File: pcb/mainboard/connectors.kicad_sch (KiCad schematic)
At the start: 20 parts, among them J28 SMPM, J29 SMPM, J30 SMPM, J31 SMPM, J32 SMPM, J33 SMPM, J34 SMPM, J35 SMPM, J36 SMPM, J37 SMPM, J38 SMPM, J39 SMPM, J40 SMPM, J41 SMPM, J42 SMPM, J43 SMPM, J44 SMPM, J45 SMPM, J46 SMPM, J47 SMPM

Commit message: Finished initial iteration of schematic, needs a verification pass to check for missing features then schematic review
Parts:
- added C209, C210, C215, C216: 0.47 uF, symbol device:C
- added C211, C212, C217, C218: 4.7 uF, symbol device:C
- added C213, C214, C219, C220: 10 uF, symbol device:C
- added K1, K2, K3, K4: RELAY_TE_HF3_96, symbol special-azonenberg:RELAY_TE_HF3_96
- added U55, U56, U57, U58: BD63573NUV, symbol special-azonenberg:BD63573NUV
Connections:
- net GND: now also C209.2, C210.2, C211.2, C212.2, C213.2, C214.2, C215.2, C216.2, C217.2, C218.2, C219.2, C220.2, K1.10 (GND), K1.13 (GND), K1.2 (GND), K1.5 (GND), K1.7 (GND), K2.10 (GND), K2.13 (GND), K2.2 (GND), K2.5 (GND), K2.7 (GND), K3.10 (GND), K3.13 (GND), K3.2 (GND), K3.5 (GND), K3.7 (GND), K4.10 (GND), K4.13 (GND), K4.2 (GND), K4.5 (GND), K4.7 (GND), U55.10 (GND), U55.5 (PGND), U55.9 (PWM), U56.10 (GND), U56.5 (PGND), U56.9 (PWM), U57.10 (GND), U57.5 (PGND), U57.9 (PWM), U58.10 (GND), U58.5 (PGND), U58.9 (PWM)
- net IN10: now also K3.14 (A)
- net IN11: now also K4.14 (A)
- net IN8: now also K1.14 (A)
- net IN9: now also K2.14 (A)
- net IO10: now also K3.6 (COM)
- net IO11: now also K4.6 (COM)
- net IO8: now also K1.6 (COM)
- net IO9: now also K2.6 (COM)
- net OUT10: now also K3.20 (B)
- net OUT11: now also K4.20 (B)
- net OUT8: now also K1.20 (B)
- net OUT9: now also K2.20 (B)
- new net: K3.15 (GND), K3.17 (GND), K3.19 (GND), K3.21 (GND)
- new net: K2.15 (GND), K2.17 (GND), K2.19 (GND), K2.21 (GND)
- new net: K4.15 (GND), K4.17 (GND), K4.19 (GND), K4.21 (GND)
- new net: K1.15 (GND), K1.17 (GND), K1.19 (GND), K1.21 (GND)
- new net 12V0: C213.1, C214.1, C219.1, C220.1, U55.7 (VM), U56.7 (VM), U57.7 (VM), U58.7 (VM)
- new net 3V3: C209.1, C210.1, C211.1, C212.1, C215.1, C216.1, C217.1, C218.1, U55.1 (PS), U55.8 (VCC), U56.1 (PS), U56.8 (VCC), U57.1 (PS), U57.8 (VCC), U58.1 (PS), U58.8 (VCC)
- new net CH10_COIL_N: K3.1 (SET1_N), K3.12 (SET2_N), U55.4 (OUTB)
- new net CH10_COIL_P: K3.11 (SET1_P), K3.22 (SET2_P), U55.6 (OUTA)
- new net CH11_COIL_N: K4.1 (SET1_N), K4.12 (SET2_N), U57.4 (OUTB)
- new net CH11_COIL_P: K4.11 (SET1_P), K4.22 (SET2_P), U57.6 (OUTA)
- new net CH8_COIL_N: K1.1 (SET1_N), K1.12 (SET2_N), U56.4 (OUTB)
- new net CH8_COIL_P: K1.11 (SET1_P), K1.22 (SET2_P), U56.6 (OUTA)
- new net CH9_COIL_N: K2.1 (SET1_N), K2.12 (SET2_N), U58.4 (OUTB)
- new net CH9_COIL_P: K2.11 (SET1_P), K2.22 (SET2_P), U58.6 (OUTA)
- new net OE10A: U55.3 (INA)
- new net OE10B: U55.2 (INB)
- new net OE11A: U57.3 (INA)
- new net OE11B: U57.2 (INB)
- new net OE8A: U56.3 (INA)
- new net OE8B: U56.2 (INB)
- new net OE9A: U58.3 (INA)
- new net OE9B: U58.2 (INB)
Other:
- note removed: "TODO: Relays or something to mux bidir ports"
- moved on the sheet: J28, J29, J30, J31, J32, J33, J34, J35, J36, J37, J38, J39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

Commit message: Calculated power monitor voltage divider
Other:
- company: (none) -> Antikernel Labs
- title: (none) -> Trigger Crossbar
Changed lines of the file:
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@@
 (kicad_sch (version 20211123) (generator eeschema)
   (paper "A4")
+  (title_block
+    (title "Trigger Crossbar")
+    (date "2023-12-17")
+    (rev "0.1")
+    (company "Antikernel Labs")
+    (comment 1 "Andrew D. Zonenberg")
+  )
   (junction (at 133.35 124.46) (diameter 0) (color 0 0 0 0)
   )

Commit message: Began assigning footprints
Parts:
- C209, C210, C215, C216: footprint (none) -> azonenberg_pcb:EIA_0402_CAP_NOSILK
- C211, C212, C217, C218: footprint (none) -> azonenberg_pcb:EIA_0603_CAP_NOSILK
- C213, C214, C219, C220: value 10 uF -> 10 uF 25V; footprint (none) -> azonenberg_pcb:EIA_1210_CAP_NOSILK
- U55, U56, U57, U58: footprint (none) -> azonenberg_pcb:DFN_10_0.5MM_3x3MM
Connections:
- net GND: now also K1.15 (GND), K1.17 (GND), K1.19 (GND), K1.21 (GND), K2.15 (GND), K2.17 (GND), K2.19 (GND), K2.21 (GND), K3.15 (GND), K3.17 (GND), K3.19 (GND), K3.21 (GND), K4.15 (GND), K4.17 (GND), K4.19 (GND), K4.21 (GND)
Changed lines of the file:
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@@
+    (effects (font (size 1.27 1.27)) (justify left bottom))
+  )
+  (label "GND" (at 204.47 55.88 0)
     (effects (font (size 1.27 1.27)) (justify left bottom))
   )
@@
     (effects (font (size 1.27 1.27)) (justify right bottom))
   )
+  (label "GND" (at 204.47 22.86 0)
+    (effects (font (size 1.27 1.27)) (justify left bottom))
+  )
   (label "GND" (at 67.31 40.64 0)
     (effects (font (size 1.27 1.27)) (justify left bottom))
@@
     (effects (font (size 1.27 1.27)) (justify left bottom))
   )
+  (label "GND" (at 142.24 55.88 0)
+    (effects (font (size 1.27 1.27)) (justify left bottom))
+  )
   (label "3V3" (at 177.8 143.51 180)
     (effects (font (size 1.27 1.27)) (justify right bottom))
@@
   )
   (label "CH11_COIL_P" (at 200.66 146.05 0)
+    (effects (font (size 1.27 1.27)) (justify left bottom))
+  )
+  (label "GND" (at 142.24 22.86 0)
     (effects (font (size 1.27 1.27)) (justify left bottom))
   )
@@
       (effects (font (size 1.27 1.27)) (justify left))
     )
-    (property "Value" "10 uF" (id 1) (at 215.011 121.0822 0)
-      (effects (font (size 1.27 1.27)) (justify left))
-    )
-    (property "Footprint" "" (id 2) (at 213.0552 123.19 0)
+    (property "Value" "10 uF 25V" (id 1) (at 215.011 121.0822 0)
+      (effects (font (size 1.27 1.27)) (justify left))
+    )
+    (property "Footprint" "azonenberg_pcb:EIA_1210_CAP_NOSILK" (id 2) (at 213.0552 123.19 0)
       (effects (font (size 1.27 1.27)) hide)
     )
@@
       (effects (font (size 1.27 1.27)) (justify left))
     )
-    (property "Value" "10 uF" (id 1) (at 213.741 160.4522 0)
-      (effects (font (size 1.27 1.27)) (justify left))
-    )
-    (property "Footprint" "" (id 2) (at 211.7852 162.56 0)
+    (property "Value" "10 uF 25V" (id 1) (at 213.741 160.4522 0)
+      (effects (font (size 1.27 1.27)) (justify left))
+    )
+    (property "Footprint" "azonenberg_pcb:EIA_1210_CAP_NOSILK" (id 2) (at 211.7852 162.56 0)
       (effects (font (size 1.27 1.27)) hide)
     )
@@
     (property "Reference" "U58" (id 0) (at 190.5 86.521 0))
     (property "Value" "BD63573NUV" (id 1) (at 190.5 89.0579 0))
-    (property "Footprint" "" (id 2) (at 182.88 114.3 0)
+    (property "Footprint" "azonenberg_pcb:DFN_10_0.5MM_3x3MM" (id 2) (at 182.88 114.3 0)
       (effects (font (size 1.27 1.27)) hide)
     )
@@
       (effects (font (size 1.27 1.27)) (justify left))
     )
-    (property "Footprint" "" (id 2) (at 133.0452 163.83 0)
+    (property "Footprint" "azonenberg_pcb:EIA_0603_CAP_NOSILK" (id 2) (at 133.0452 163.83 0)
       (effects (font (size 1.27 1.27)) hide)
     )
@@
       (effects (font (size 1.27 1.27)) (justify left))
     )
-    (property "Value" "10 uF" (id 1) (at 152.781 122.3522 0)
-      (effects (font (size 1.27 1.27)) (justify left))
-    )
-    (property "Footprint" "" (id 2) (at 150.8252 124.46 0)
+    (property "Value" "10 uF 25V" (id 1) (at 152.781 122.3522 0)
+      (effects (font (size 1.27 1.27)) (justify left))
+    )
+    (property "Footprint" "azonenberg_pcb:EIA_1210_CAP_NOSILK" (id 2) (at 150.8252 124.46 0)
       (effects (font (size 1.27 1.27)) hide)
     )
@@
       (effects (font (size 1.27 1.27)) (justify left))
     )
-    (property "Footprint" "" (id 2) (at 120.3452 163.83 0)
+    (property "Footprint" "azonenberg_pcb:EIA_0402_CAP_NOSILK" (id 2) (at 120.3452 163.83 0)
       (effects (font (size 1.27 1.27)) hide)
     )
@@
     (property "Reference" "U55" (id 0) (at 127 127.161 0))
     (property "Value" "BD63573NUV" (id 1) (at 127 129.6979 0))
-    (property "Footprint" "" (id 2) (at 119.38 154.94 0)
+    (property "Footprint" "azonenberg_pcb:DFN_10_0.5MM_3x3MM" (id 2) (at 119.38 154.94 0)
       (effects (font (size 1.27 1.27)) hide)
     )
@@
       (effects (font (size 1.27 1.27)) (justify left))
     )
-    (property "Footprint" "" (id 2) (at 195.2752 162.56 0)
+    (property "Footprint" "azonenberg_pcb:EIA_0603_CAP_NOSILK" (id 2) (at 195.2752 162.56 0)
       (effects (font (size 1.27 1.27)) hide)
     )
@@
       (effects (font (size 1.27 1.27)) (justify left))
     )
-    (property "Footprint" "" (id 2) (at 134.3152 124.46 0)
+    (property "Footprint" "azonenberg_pcb:EIA_0603_CAP_NOSILK" (id 2) (at 134.3152 124.46 0)
       (effects (font (size 1.27 1.27)) hide)
     )
@@
       (effects (font (size 1.27 1.27)) (justify left))
     )
-    (property "Footprint" "" (id 2) (at 182.5752 162.56 0)
+    (property "Footprint" "azonenberg_pcb:EIA_0402_CAP_NOSILK" (id 2) (at 182.5752 162.56 0)
       (effects (font (size 1.27 1.27)) hide)
     )
@@
     (property "Reference" "U57" (id 0) (at 189.23 125.891 0))
     (property "Value" "BD63573NUV" (id 1) (at 189.23 128.4279 0))
-    (property "Footprint" "" (id 2) (at 181.61 153.67 0)
+    (property "Footprint" "azonenberg_pcb:DFN_10_0.5MM_3x3MM" (id 2) (at 181.61 153.67 0)
       (effects (font (size 1.27 1.27)) hide)
     )
@@
       (effects (font (size 1.27 1.27)) (justify left))
     )
-    (property "Footprint" "" (id 2) (at 196.5452 123.19 0)
+    (property "Footprint" "azonenberg_pcb:EIA_0603_CAP_NOSILK" (id 2) (at 196.5452 123.19 0)
       (effects (font (size 1.27 1.27)) hide)
     )
@@
       (effects (font (size 1.27 1.27)) (justify left))
     )
-    (property "Footprint" "" (id 2) (at 121.6152 124.46 0)
+    (property "Footprint" "azonenberg_pcb:EIA_0402_CAP_NOSILK" (id 2) (at 121.6152 124.46 0)
       (effects (font (size 1.27 1.27)) hide)
     )
@@
       (effects (font (size 1.27 1.27)) (justify left))
     )
-    (property "Footprint" "" (id 2) (at 183.8452 123.19 0)
+    (property "Footprint" "azonenberg_pcb:EIA_0402_CAP_NOSILK" (id 2) (at 183.8452 123.19 0)
       (effects (font (size 1.27 1.27)) hide)
     )
@@
       (effects (font (size 1.27 1.27)) (justify left))
     )
-    (property "Value" "10 uF" (id 1) (at 151.511 161.7222 0)
-      (effects (font (size 1.27 1.27)) (justify left))
-    )
-    (property "Footprint" "" (id 2) (at 149.5552 163.83 0)
+    (property "Value" "10 uF 25V" (id 1) (at 151.511 161.7222 0)
+      (effects (font (size 1.27 1.27)) (justify left))
+    )
+    (property "Footprint" "azonenberg_pcb:EIA_1210_CAP_NOSILK" (id 2) (at 149.5552 163.83 0)
       (effects (font (size 1.27 1.27)) hide)
     )
@@
     (property "Reference" "U56" (id 0) (at 128.27 87.791 0))
     (property "Value" "BD63573NUV" (id 1) (at 128.27 90.3279 0))
-    (property "Footprint" "" (id 2) (at 120.65 115.57 0)
-      (effects (font (size 1.27 1.27)) hide)
-    )
+    (property "Footprint" "azonenberg_pcb:DFN_10_0.5MM_3x3MM" (id 2) (at 120.65 115.57 0)
+      (effects (font (size 1.27 1.27)) hide)
+    )

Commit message: Finished component footprint assignment, started some EM simulations. Ready for schematic review.
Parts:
- J28, J29, J30, J31, J32, J33, J34, J35, J36, J37, J38, J39, J40, J41, J42, J43, J44, J45, J46, J47: footprint (none) -> azonenberg_pcb:CONN_SMPM_AMPHENOL_C925-197J-51PT
- K1, K2, K3, K4: footprint (none) -> azonenberg_pcb:RELAY_TE_HF3_2COIL_50OHM
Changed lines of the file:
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@@
   (title_block
     (title "Trigger Crossbar")
-    (date "2023-12-17")
+    (date "2023-12-18")
     (rev "0.1")
     (company "Antikernel Labs")
@@
     (property "Reference" "K3" (id 0) (at 191.77 17.941 0))
     (property "Value" "RELAY_TE_HF3_96" (id 1) (at 191.77 20.4779 0))
-    (property "Footprint" "" (id 2) (at 182.88 48.26 0)
+    (property "Footprint" "azonenberg_pcb:RELAY_TE_HF3_2COIL_50OHM" (id 2) (at 182.88 48.26 0)
       (effects (font (size 1.27 1.27)) hide)
     )
@@
     (property "Reference" "J34" (id 0) (at 35.5599 44.0036 0))
     (property "Value" "SMPM" (id 1) (at 35.5599 46.5405 0))
-    (property "Footprint" "" (id 2) (at 35.56 49.53 0)
+    (property "Footprint" "azonenberg_pcb:CONN_SMPM_AMPHENOL_C925-197J-51PT" (id 2) (at 35.56 49.53 0)
       (effects (font (size 1.27 1.27)) hide)
     )
@@
     (property "Reference" "J40" (id 0) (at 21.5899 74.4836 0))
     (property "Value" "SMPM" (id 1) (at 21.5899 77.0205 0))
-    (property "Footprint" "" (id 2) (at 21.59 80.01 0)
+    (property "Footprint" "azonenberg_pcb:CONN_SMPM_AMPHENOL_C925-197J-51PT" (id 2) (at 21.59 80.01 0)
       (effects (font (size 1.27 1.27)) hide)
     )
@@
     (property "Reference" "J28" (id 0) (at 21.5899 16.0636 0))
     (property "Value" "SMPM" (id 1) (at 21.5899 18.6005 0))
-    (property "Footprint" "" (id 2) (at 21.59 21.59 0)
+    (property "Footprint" "azonenberg_pcb:CONN_SMPM_AMPHENOL_C925-197J-51PT" (id 2) (at 21.59 21.59 0)
       (effects (font (size 1.27 1.27)) hide)
     )
@@
     (property "Reference" "J32" (id 0) (at 35.5599 16.0636 0))
     (property "Value" "SMPM" (id 1) (at 35.5599 18.6005 0))
-    (property "Footprint" "" (id 2) (at 35.56 21.59 0)
+    (property "Footprint" "azonenberg_pcb:CONN_SMPM_AMPHENOL_C925-197J-51PT" (id 2) (at 35.56 21.59 0)
       (effects (font (size 1.27 1.27)) hide)
     )
@@
     (property "Reference" "J45" (id 0) (at 50.7999 88.4536 0))
     (property "Value" "SMPM" (id 1) (at 50.7999 90.9905 0))
-    (property "Footprint" "" (id 2) (at 50.8 93.98 0)
+    (property "Footprint" "azonenberg_pcb:CONN_SMPM_AMPHENOL_C925-197J-51PT" (id 2) (at 50.8 93.98 0)
       (effects (font (size 1.27 1.27)) hide)
     )
@@
     (property "Reference" "J44" (id 0) (at 50.7999 74.4836 0))
     (property "Value" "SMPM" (id 1) (at 50.7999 77.0205 0))
-    (property "Footprint" "" (id 2) (at 50.8 80.01 0)
+    (property "Footprint" "azonenberg_pcb:CONN_SMPM_AMPHENOL_C925-197J-51PT" (id 2) (at 50.8 80.01 0)
       (effects (font (size 1.27 1.27)) hide)
     )
@@
     (property "Reference" "J31" (id 0) (at 21.5899 57.9736 0))
     (property "Value" "SMPM" (id 1) (at 21.5899 60.5105 0))
-    (property "Footprint" "" (id 2) (at 21.59 63.5 0)
+    (property "Footprint" "azonenberg_pcb:CONN_SMPM_AMPHENOL_C925-197J-51PT" (id 2) (at 21.59 63.5 0)
       (effects (font (size 1.27 1.27)) hide)
     )
@@
     (property "Reference" "J43" (id 0) (at 35.5599 88.4536 0))
     (property "Value" "SMPM" (id 1) (at 35.5599 90.9905 0))
-    (property "Footprint" "" (id 2) (at 35.56 93.98 0)
+    (property "Footprint" "azonenberg_pcb:CONN_SMPM_AMPHENOL_C925-197J-51PT" (id 2) (at 35.56 93.98 0)
       (effects (font (size 1.27 1.27)) hide)
     )
@@
     (property "Reference" "J41" (id 0) (at 21.5899 88.4536 0))
     (property "Value" "SMPM" (id 1) (at 21.5899 90.9905 0))
-    (property "Footprint" "" (id 2) (at 21.59 93.98 0)
+    (property "Footprint" "azonenberg_pcb:CONN_SMPM_AMPHENOL_C925-197J-51PT" (id 2) (at 21.59 93.98 0)
       (effects (font (size 1.27 1.27)) hide)
     )
@@
     (property "Reference" "J37" (id 0) (at 49.5299 30.0336 0))
     (property "Value" "SMPM" (id 1) (at 49.5299 32.5705 0))
-    (property "Footprint" "" (id 2) (at 49.53 35.56 0)
+    (property "Footprint" "azonenberg_pcb:CONN_SMPM_AMPHENOL_C925-197J-51PT" (id 2) (at 49.53 35.56 0)
       (effects (font (size 1.27 1.27)) hide)
     )
@@
     (property "Reference" "J35" (id 0) (at 35.5599 57.9736 0))
     (property "Value" "SMPM" (id 1) (at 35.5599 60.5105 0))
-    (property "Footprint" "" (id 2) (at 35.56 63.5 0)
+    (property "Footprint" "azonenberg_pcb:CONN_SMPM_AMPHENOL_C925-197J-51PT" (id 2) (at 35.56 63.5 0)
       (effects (font (size 1.27 1.27)) hide)
     )
@@
     (property "Reference" "J36" (id 0) (at 49.5299 16.0636 0))
     (property "Value" "SMPM" (id 1) (at 49.5299 18.6005 0))
-    (property "Footprint" "" (id 2) (at 49.53 21.59 0)
+    (property "Footprint" "azonenberg_pcb:CONN_SMPM_AMPHENOL_C925-197J-51PT" (id 2) (at 49.53 21.59 0)
       (effects (font (size 1.27 1.27)) hide)
     )
@@
     (property "Reference" "J46" (id 0) (at 63.4999 74.4836 0))
     (property "Value" "SMPM" (id 1) (at 63.4999 77.0205 0))
-    (property "Footprint" "" (id 2) (at 63.5 80.01 0)
+    (property "Footprint" "azonenberg_pcb:CONN_SMPM_AMPHENOL_C925-197J-51PT" (id 2) (at 63.5 80.01 0)
       (effects (font (size 1.27 1.27)) hide)
     )
@@
     (property "Reference" "J29" (id 0) (at 21.5899 30.0336 0))
     (property "Value" "SMPM" (id 1) (at 21.5899 32.5705 0))
-    (property "Footprint" "" (id 2) (at 21.59 35.56 0)
+    (property "Footprint" "azonenberg_pcb:CONN_SMPM_AMPHENOL_C925-197J-51PT" (id 2) (at 21.59 35.56 0)
       (effects (font (size 1.27 1.27)) hide)
     )
@@
     (property "Reference" "J42" (id 0) (at 35.5599 74.4836 0))
     (property "Value" "SMPM" (id 1) (at 35.5599 77.0205 0))
-    (property "Footprint" "" (id 2) (at 35.56 80.01 0)
+    (property "Footprint" "azonenberg_pcb:CONN_SMPM_AMPHENOL_C925-197J-51PT" (id 2) (at 35.56 80.01 0)
       (effects (font (size 1.27 1.27)) hide)
     )
@@
     (property "Reference" "J30" (id 0) (at 21.5899 44.0036 0))
     (property "Value" "SMPM" (id 1) (at 21.5899 46.5405 0))
-    (property "Footprint" "" (id 2) (at 21.59 49.53 0)
+    (property "Footprint" "azonenberg_pcb:CONN_SMPM_AMPHENOL_C925-197J-51PT" (id 2) (at 21.59 49.53 0)
       (effects (font (size 1.27 1.27)) hide)
     )
@@
     (property "Reference" "K2" (id 0) (at 129.54 50.961 0))
     (property "Value" "RELAY_TE_HF3_96" (id 1) (at 129.54 53.4979 0))
-    (property "Footprint" "" (id 2) (at 120.65 81.28 0)
+    (property "Footprint" "azonenberg_pcb:RELAY_TE_HF3_2COIL_50OHM" (id 2) (at 120.65 81.28 0)
       (effects (font (size 1.27 1.27)) hide)
     )
@@
     (property "Reference" "K4" (id 0) (at 191.77 50.961 0))
     (property "Value" "RELAY_TE_HF3_96" (id 1) (at 191.77 53.4979 0))
-    (property "Footprint" "" (id 2) (at 182.88 81.28 0)
+    (property "Footprint" "azonenberg_pcb:RELAY_TE_HF3_2COIL_50OHM" (id 2) (at 182.88 81.28 0)
       (effects (font (size 1.27 1.27)) hide)
     )
@@
     (property "Reference" "J39" (id 0) (at 63.4999 30.0336 0))
     (property "Value" "SMPM" (id 1) (at 63.4999 32.5705 0))
-    (property "Footprint" "" (id 2) (at 63.5 35.56 0)
+    (property "Footprint" "azonenberg_pcb:CONN_SMPM_AMPHENOL_C925-197J-51PT" (id 2) (at 63.5 35.56 0)
       (effects (font (size 1.27 1.27)) hide)
     )
@@
     (property "Reference" "J38" (id 0) (at 63.4999 16.0636 0))
     (property "Value" "SMPM" (id 1) (at 63.4999 18.6005 0))
-    (property "Footprint" "" (id 2) (at 63.5 21.59 0)
+    (property "Footprint" "azonenberg_pcb:CONN_SMPM_AMPHENOL_C925-197J-51PT" (id 2) (at 63.5 21.59 0)
       (effects (font (size 1.27 1.27)) hide)
     )
@@
     (property "Reference" "K1" (id 0) (at 129.54 17.941 0))
     (property "Value" "RELAY_TE_HF3_96" (id 1) (at 129.54 20.4779 0))
-    (property "Footprint" "" (id 2) (at 120.65 48.26 0)
+    (property "Footprint" "azonenberg_pcb:RELAY_TE_HF3_2COIL_50OHM" (id 2) (at 120.65 48.26 0)
       (effects (font (size 1.27 1.27)) hide)
     )
@@
     (property "Reference" "J33" (id 0) (at 35.5599 30.0336 0))
     (property "Value" "SMPM" (id 1) (at 35.5599 32.5705 0))
-    (property "Footprint" "" (id 2) (at 35.56 35.56 0)
+    (property "Footprint" "azonenberg_pcb:CONN_SMPM_AMPHENOL_C925-197J-51PT" (id 2) (at 35.56 35.56 0)
       (effects (font (size 1.27 1.27)) hide)
     )
@@
     (property "Reference" "J47" (id 0) (at 63.4999 88.4536 0))
     (property "Value" "SMPM" (id 1) (at 63.4999 90.9905 0))
-    (property "Footprint" "" (id 2) (at 63.5 93.98 0)
-      (effects (font (size 1.27 1.27)) hide)
-    )
+    (property "Footprint" "azonenberg_pcb:CONN_SMPM_AMPHENOL_C925-197J-51PT" (id 2) (at 63.5 93.98 0)
+      (effects (font (size 1.27 1.27)) hide)
+    )

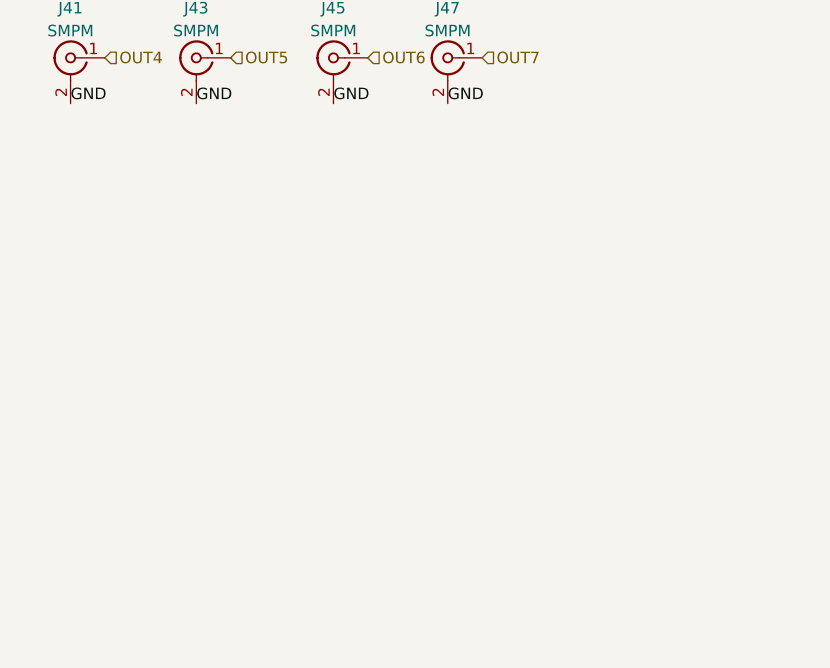
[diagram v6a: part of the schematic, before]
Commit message: Started layout of rear panel IO connectors and associated drivers/comparators
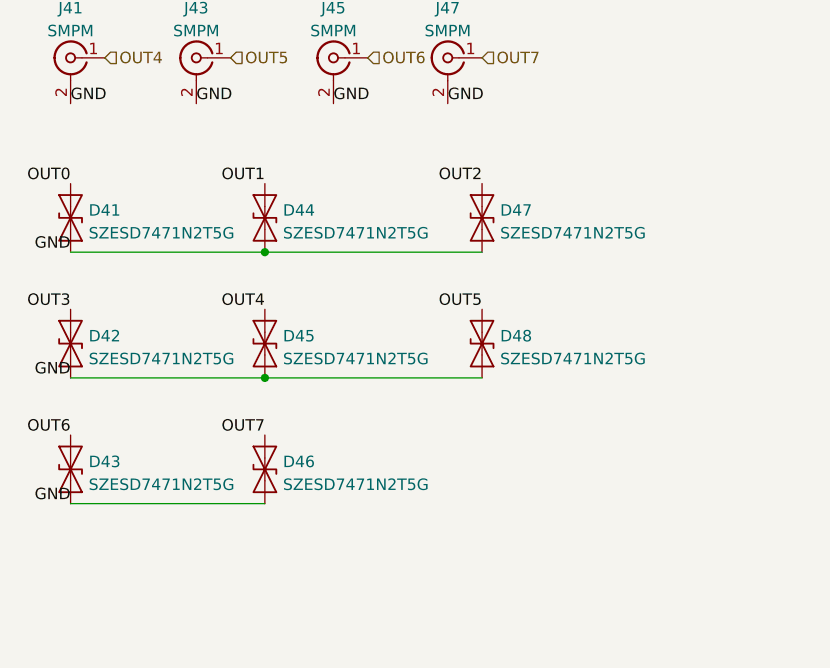
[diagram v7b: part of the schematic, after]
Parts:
- added D41, D42, D43, D44, D45, D46, D47, D48: SZESD7471N2T5G, azonenberg_pcb:SOD882, symbol device:D_TVS
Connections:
- net GND: now also D41.1 (A1), D42.1 (A1), D43.1 (A1), D44.1 (A1), D45.1 (A1), D46.1 (A1), D47.1 (A1), D48.1 (A1)
- net OUT0: now also D41.2 (A2)
- net OUT1: now also D44.2 (A2)
- net OUT2: now also D47.2 (A2)
- net OUT3: now also D42.2 (A2)
- net OUT4: now also D45.2 (A2)
- net OUT5: now also D48.2 (A2)
- net OUT6: now also D43.2 (A2)
- net OUT7: now also D46.2 (A2)
